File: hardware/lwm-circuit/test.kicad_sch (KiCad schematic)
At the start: 33 parts, among them J1 Analog, J2 Digital, U1 MCP23017x-x-ML, U2 MCP23017x-x-ML, U3 MCP23017x-x-ML, U4 MCP23017x-x-ML, U5 MCP23017x-x-ML

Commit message: Updated files
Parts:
- added J4: Micro_SD_Card_Det_Hirose_DM3AT, symbol Connector:Micro_SD_Card_Det_Hirose_DM3AT
- added U6: 254, 254:MODULE_254, symbol 254:254
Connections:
- net +5V: now also J4.4 (VDD)
- net DIR: no longer U1.17 (GPA0)
- net ENABLE: no longer U1.21 (GPA4)
- net GND: now also JP10.4, JP10.5, JP11.4, JP11.5, JP12.4, JP12.5, JP13.4, JP13.5, JP14.4, JP14.5, JP15.4, JP15.5, JP16.4, JP16.5, JP17.4, JP17.5, JP18.4, JP18.5, JP19.4, JP19.5, JP4.4, JP4.5, JP5.4, JP5.5, JP6.4, JP6.5, JP7.4, JP7.5, JP8.4, JP8.5, JP9.4, JP9.5, J4.6 (VSS); no longer JP4.2, JP5.2
- net MS2: no longer U1.20 (GPA3)
- net D8 renamed MOSI
- net MOSI: now also J4.3 (CMD)
- removed net MS1: JP10.5, JP11.5, JP12.5, JP13.5, JP14.5, JP15.5, JP16.5, JP17.5, JP18.5, JP19.5, JP4.5, JP5.5, JP6.5, JP7.5, JP8.5, JP9.5, U1.19 (GPA2)
- removed net STEP: JP10.4, JP11.4, JP12.4, JP13.4, JP14.4, JP15.4, JP16.4, JP17.4, JP18.4, JP19.4, JP4.4, JP5.4, JP6.4, JP7.4, JP8.4, JP9.4, U1.18 (GPA1)
- new net CS: J4.2 (DAT3/CD)
- new net SCLK: J4.5 (CLK)

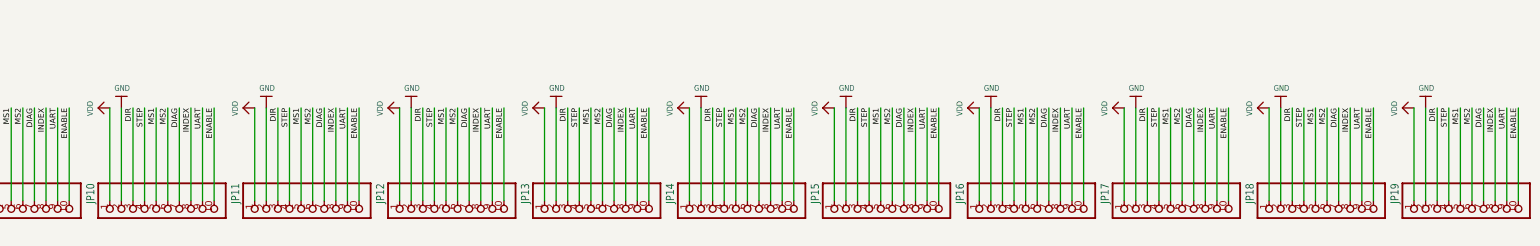
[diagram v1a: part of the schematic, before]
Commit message: removed unnessary stepper motors
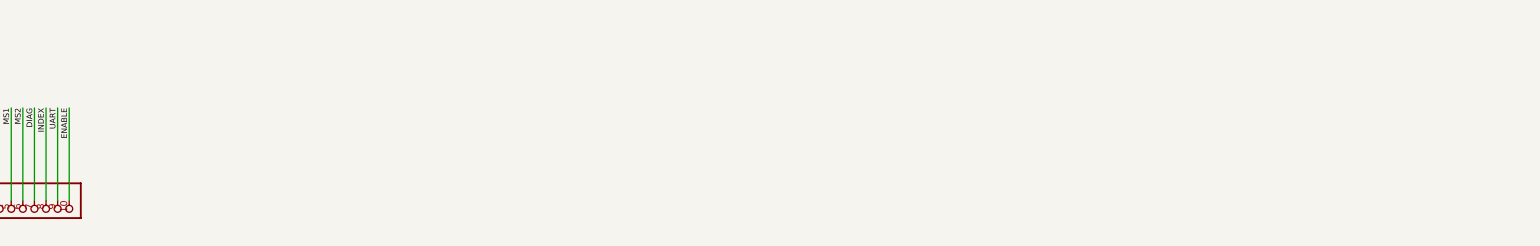
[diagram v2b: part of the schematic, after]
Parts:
- removed JP10, JP11, JP12, JP13, JP14, JP15, JP16, JP17, JP18, JP19: HEADER-1X1070MIL, Adafruit TMC2209 Stepper Motor Driver:1X10_ROUND70, symbol Adafruit TMC2209 Stepper Motor Driver-eagle-import:HEADER-1X1070MIL

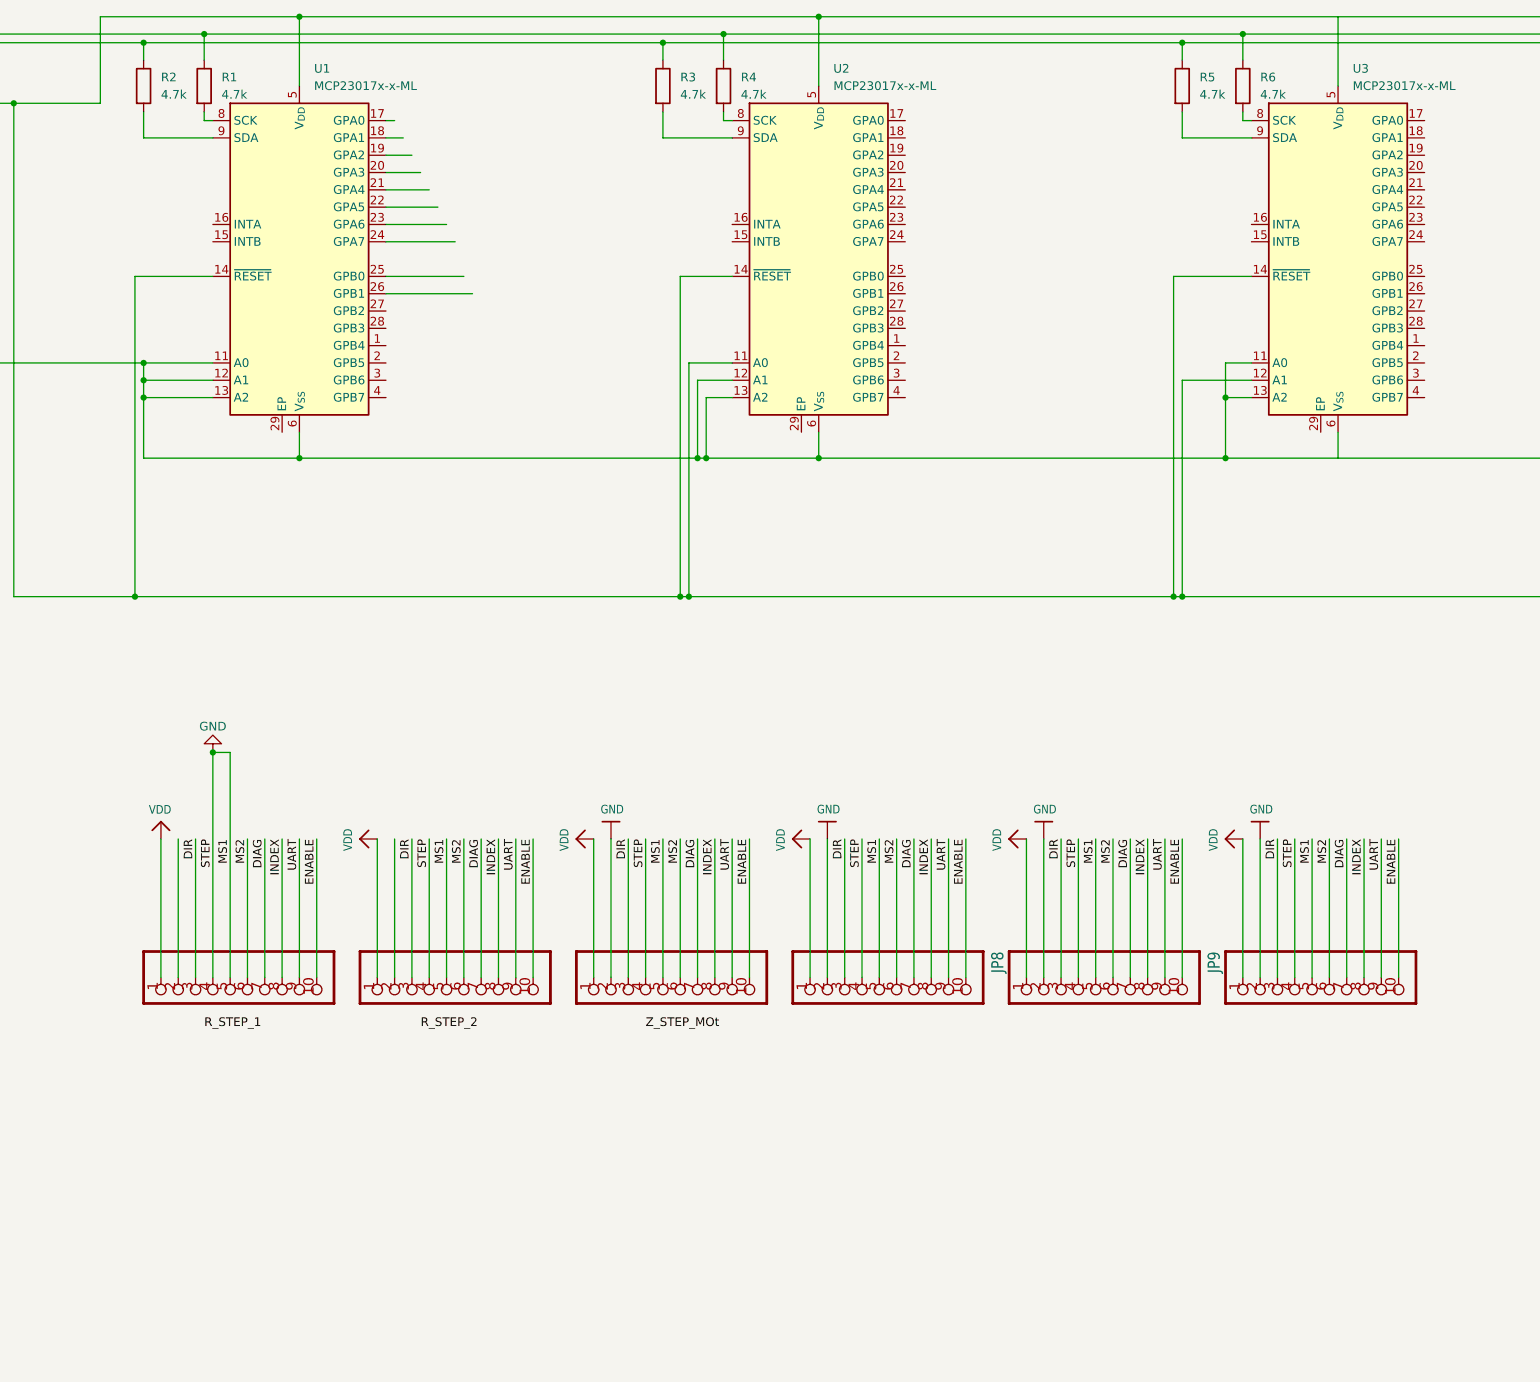
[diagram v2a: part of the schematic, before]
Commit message: Added full labels to drivers
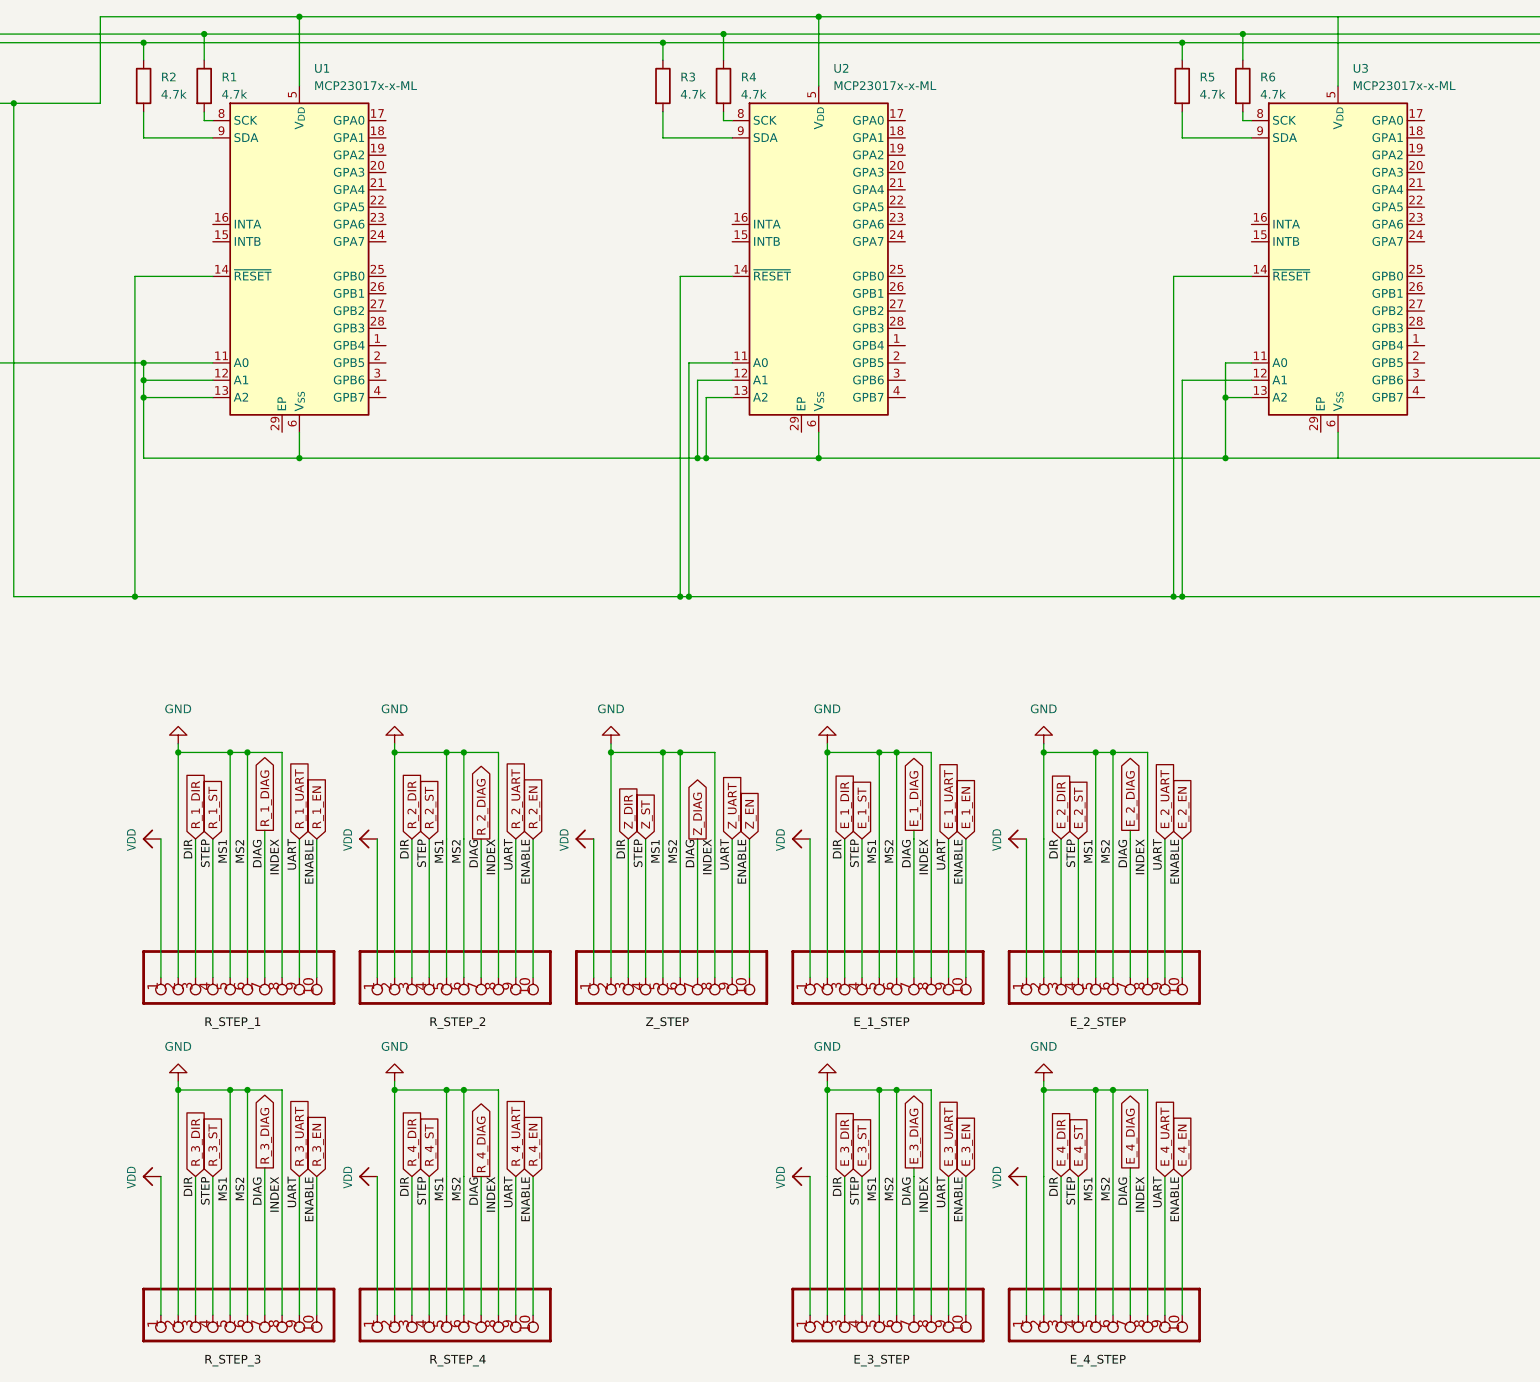
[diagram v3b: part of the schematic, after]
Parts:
- removed JP9: HEADER-1X1070MIL, Adafruit TMC2209 Stepper Motor Driver:1X10_ROUND70, symbol Adafruit TMC2209 Stepper Motor Driver-eagle-import:HEADER-1X1070MIL
- added JP10, JP11, JP12, JP13: HEADER-1X1070MIL, Adafruit TMC2209 Stepper Motor Driver:1X10_ROUND70, symbol Adafruit TMC2209 Stepper Motor Driver-eagle-import:HEADER-1X1070MIL
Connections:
- net INDEX is gone; now on net GND: JP4.8, JP5.8, JP6.8, JP7.8, JP8.8
- net MS2 is gone; now on net GND: JP4.6, JP5.6, JP6.6, JP7.6, JP8.6
- net GND: now also JP4.2, JP5.2, JP10.2, JP10.5, JP10.6, JP10.8, JP11.2, JP11.5, JP11.6, JP11.8, JP12.2, JP12.5, JP12.6, JP12.8, JP13.2, JP13.5, JP13.6, JP13.8; no longer JP4.4, JP5.4, JP6.4, JP7.4, JP8.4
- net VDD: now also JP10.1, JP11.1, JP12.1, JP13.1
- net DIAG renamed E_1_DIAG
- net E_1_DIAG: now also JP10.7, JP11.7, JP12.7, JP13.7
- net DIR renamed E_1_DIR
- net E_1_DIR: now also JP10.3, JP11.3, JP12.3, JP13.3
- net ENABLE renamed E_1_EN
- net E_1_EN: now also JP10.10, JP11.10, JP12.10, JP13.10
- net UART renamed E_1_UART
- net E_1_UART: now also JP10.9, JP11.9, JP12.9, JP13.9
- new net E_1_ST: JP10.4, JP11.4, JP12.4, JP13.4, JP4.4, JP5.4, JP6.4, JP7.4, JP8.4
